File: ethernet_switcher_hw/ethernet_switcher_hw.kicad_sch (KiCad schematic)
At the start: 0 parts

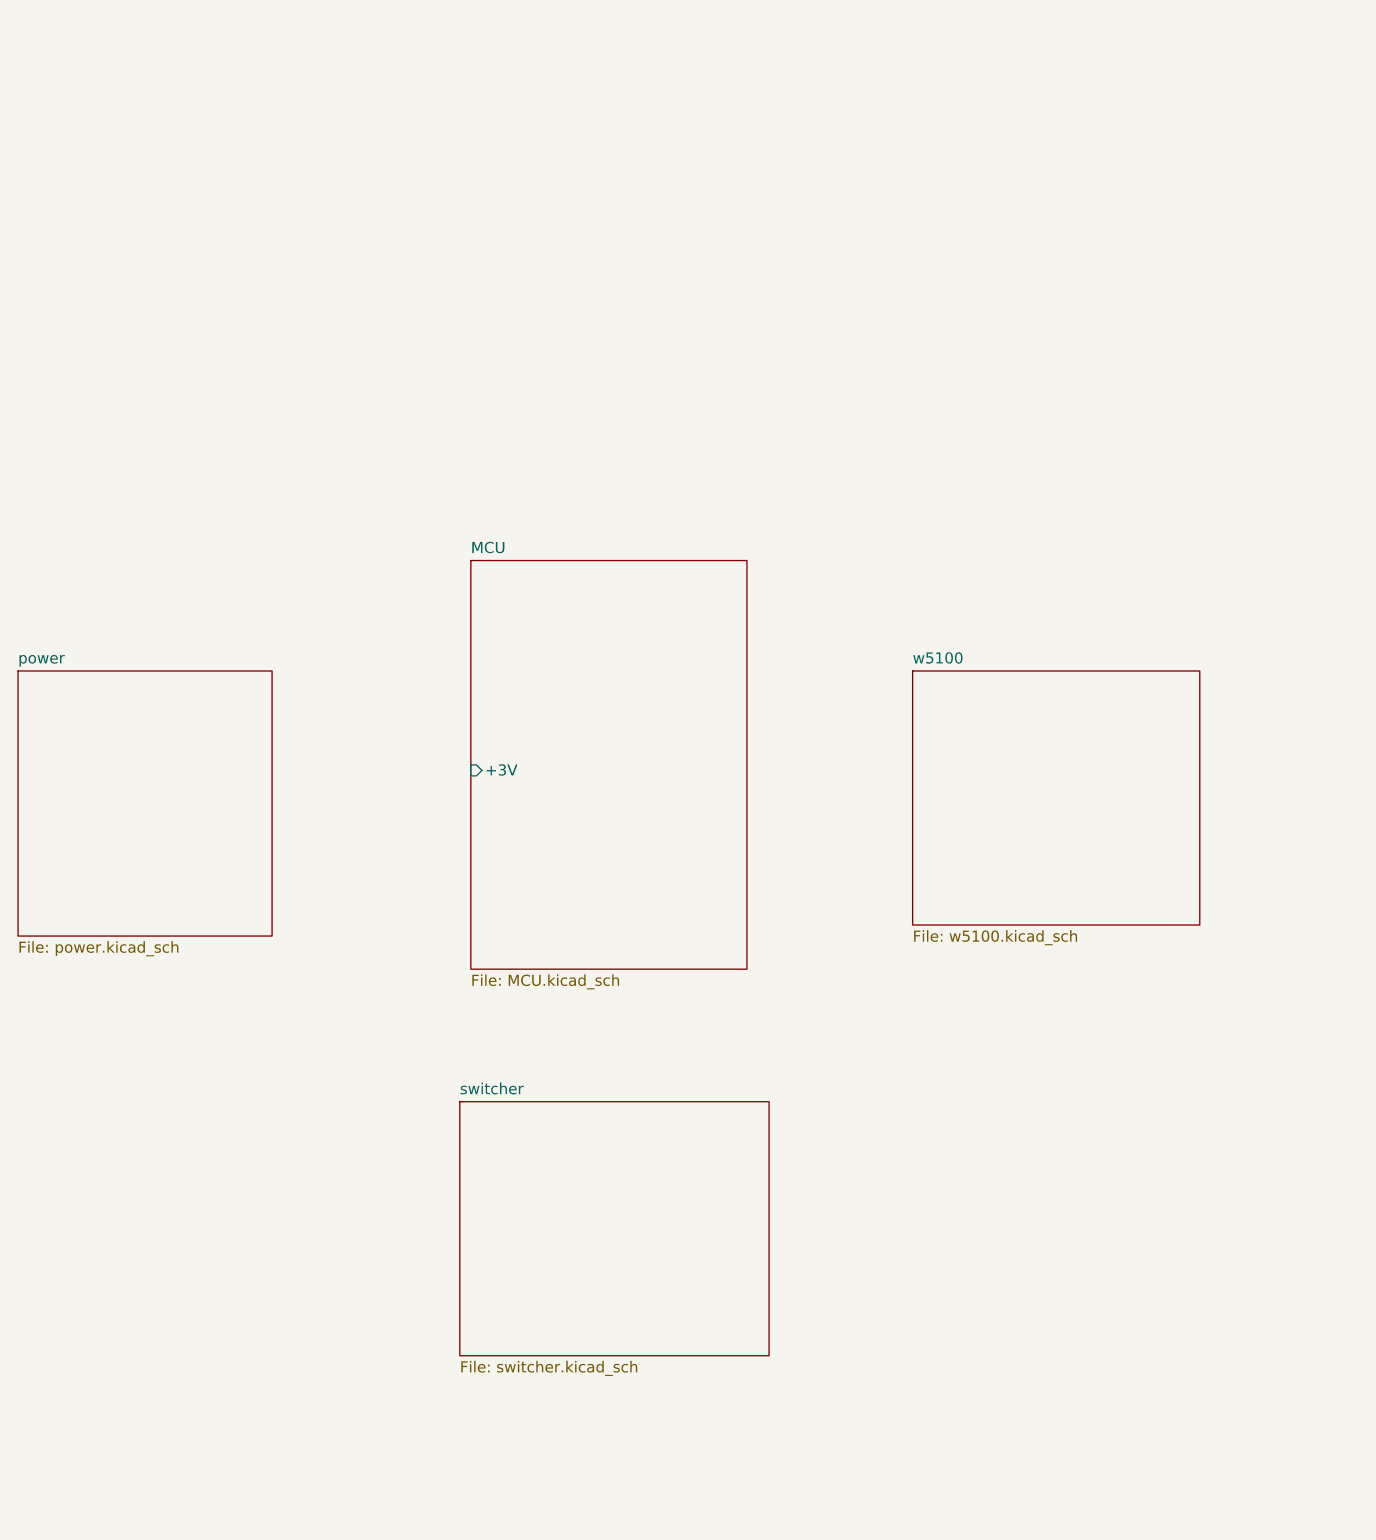
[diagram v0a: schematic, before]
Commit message: timer works incorrectly. It's clocked from slower source
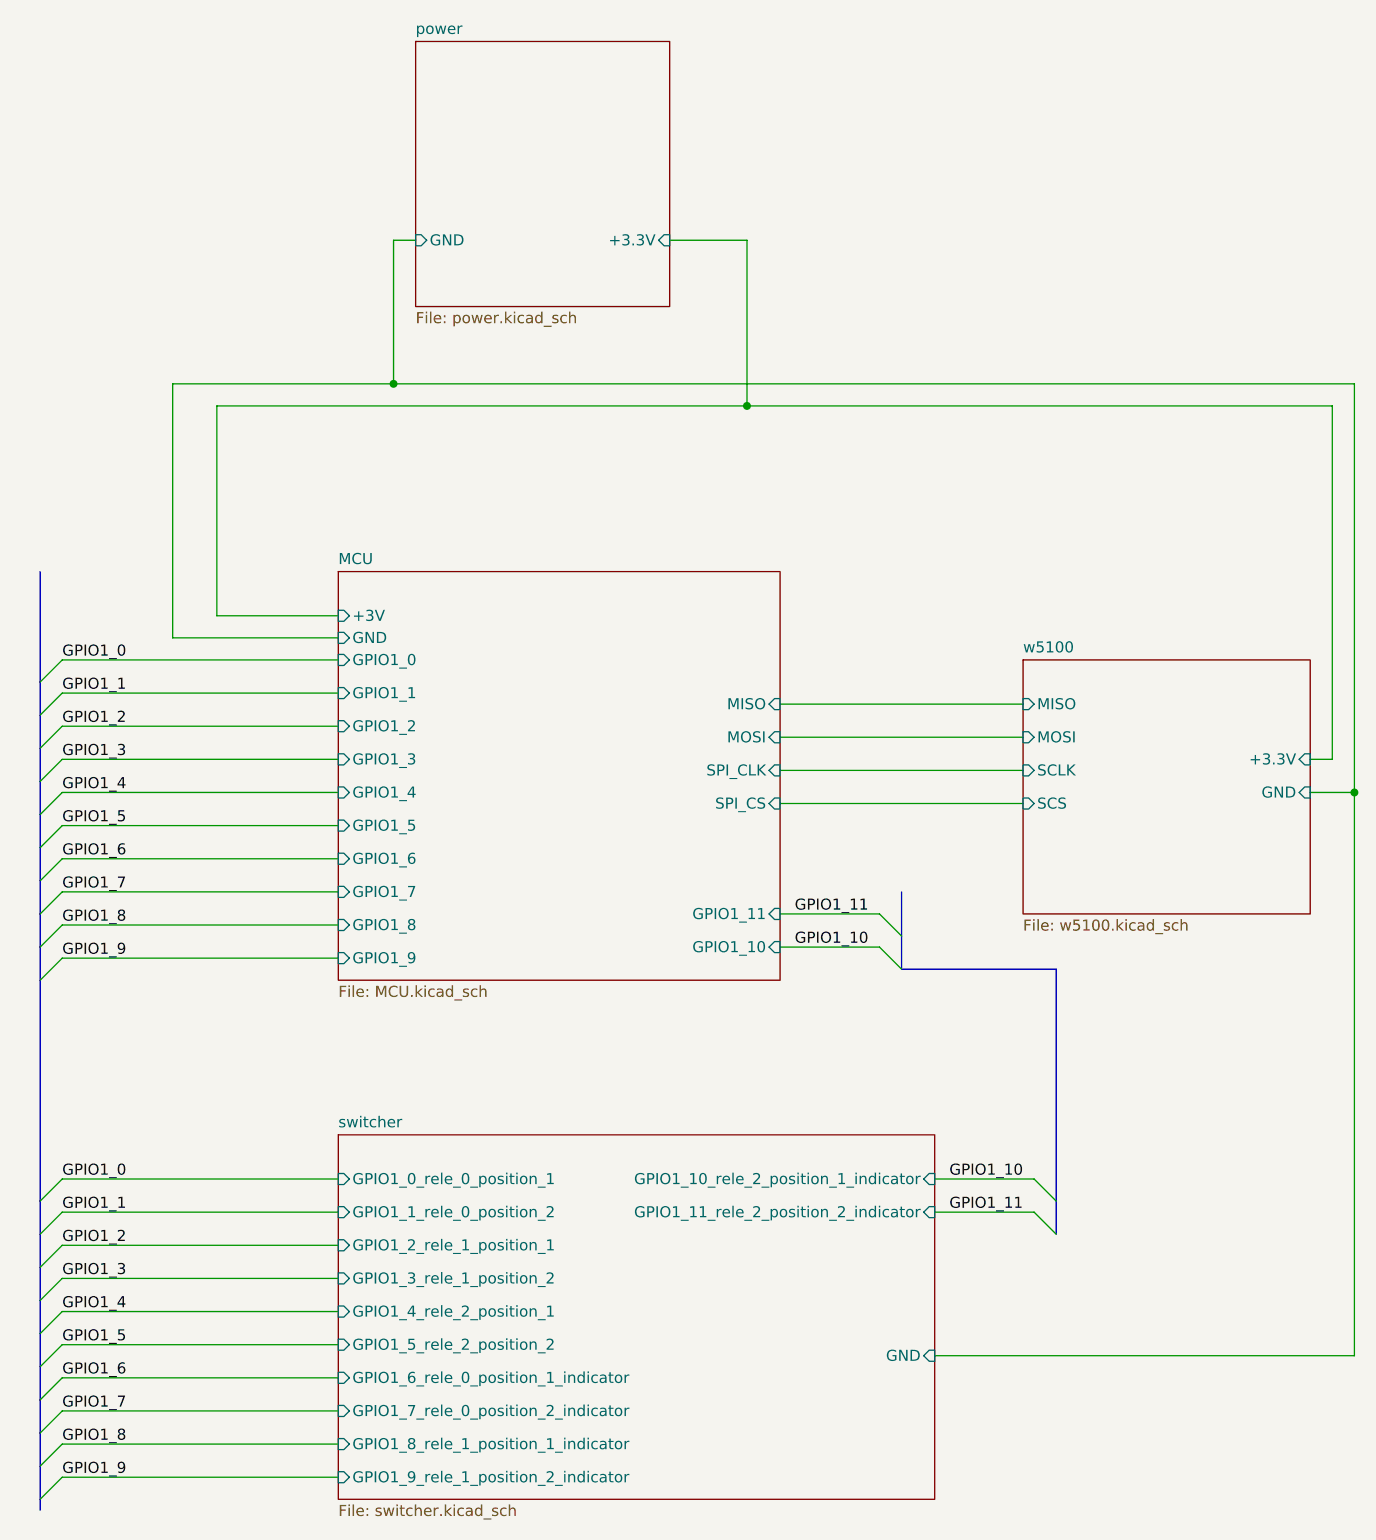
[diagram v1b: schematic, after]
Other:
- sheet MCU ports: added GND, GPIO1_0, GPIO1_1, GPIO1_10, GPIO1_11, GPIO1_2, GPIO1_3, GPIO1_4, GPIO1_5, GPIO1_6, GPIO1_7, GPIO1_8, GPIO1_9, MISO, MOSI, SPI_CLK, SPI_CS; removed none
- sheet power ports: added +3.3V, GND; removed none
- sheet switcher ports: added GND, GPIO1_0_rele_0_position_1, GPIO1_10_rele_2_position_1_indicator, GPIO1_11_rele_2_position_2_indicator, GPIO1_1_rele_0_position_2, GPIO1_2_rele_1_position_1, GPIO1_3_rele_1_position_2, GPIO1_4_rele_2_position_1, GPIO1_5_rele_2_position_2, GPIO1_6_rele_0_position_1_indicator, GPIO1_7_rele_0_position_2_indicator, GPIO1_8_rele_1_position_1_indicator, GPIO1_9_rele_1_position_2_indicator; removed none
- sheet w5100 ports: added +3.3V, GND, MISO, MOSI, SCLK, SCS; removed none

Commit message: 1.0.0. version of scheme
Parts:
- added A1: w5100_shield, forShields_footprints:forW5100Shield, symbol MIK32 Amur:w5100_shield
- added A2: MIK32 Amur, forShields_footprints:dip_MIK32_Amur, symbol MIK32 Amur:MIK32_Amur_DIP_Debug_PCB
- added C1: 680u, Capacitor_THT:CP_Radial_D16.0mm_P7.50mm, symbol Device:C_Polarized
- added C2: 330u, Capacitor_Tantalum_SMD:CP_EIA-7343-31_Kemet-D, symbol Device:C_Polarized
- added C3, C5: 0.1u, Capacitor_SMD:C_1206_3216Metric, symbol Device:C
- added C4, C6: 10u, Capacitors:CAP_1206, symbol Device:C_Polarized
- added D1: SMBJ30A, Diode_SMD:D_SMB, symbol Device:D
- added D10, D11, D12, D13, D14, D15, D16, D17, D18, D19, D20, D21, D22, D3, D4, D5, D6, D7, D8, D9: 1N4148WS, Diode_SMD:D_SOD-323F, symbol Device:D_Small
- added D2: 1N5824, Diode_THT:D_DO-201AD_P15.24mm_Horizontal, symbol Diode:1N5820
- added DD1, DD2, DD5: SN74LVCZ244APWR, Package_SO:SSOP-20_4.4x6.5mm_P0.65mm, symbol SN74LVCZ244APWR:SN74LVCZ244APWR
- added DD3: LM2596S-5.0, LM2596:LM2596SXADJ, symbol LM2596S-ADJ:LM2596S-ADJ
- added DD4: AMS1117-3.3, Package_TO_SOT_SMD:SOT-223-3_TabPin2, symbol Regulator_Linear:AMS1117-3.3
- added DD6, DD7, DD8: 74HC165, Package_SO:SOIC-16_3.9x9.9mm_P1.27mm, symbol 74xx:74HC165
- added F1: Fuse, Fuse:Fuse_0603_1608Metric, symbol Device:Fuse
- added L1: 47u, Inductor_SMD:L_12x12mm_H8mm, symbol Device:L
- added Q1, Q10, Q11, Q12, Q13, Q14, Q15, Q16, Q17, Q18, Q19, Q2, Q20, Q3, Q4, Q5, Q6, Q7, Q8, Q9: BSS138, Package_TO_SOT_SMD:SOT-23, symbol Transistor_FET:BSS138
- added R1, R12, R13, R15, R17, R20, R21, R23, R25, R28, R29, R3, R31, R33, R35, R37, R38, R5, R8, R9: 10k, Resistor_SMD:R_0603_1608Metric, symbol Device:R
- added R10, R11, R14, R16, R18, R19, R2, R22, R24, R26, R27, R30, R32, R34, R36, R39, R4, R40, R6, R7: 100k, Resistor_SMD:R_0603_1608Metric, symbol Device:R
- added R41: 20k, Resistor_SMD:R_0603_1608Metric, symbol Device:R
- added X1: Screw_Terminal_01x02, TerminalBlock_Phoenix:TerminalBlock_Phoenix_MKDS-1,5-2-5.08_1x02_P5.08mm_Horizontal, symbol Connector:Screw_Terminal_01x02
- added X2: ~, Connector_PinHeader_2.54mm:PinHeader_2x15_P2.54mm_Vertical, symbol MIK32 Amur:Connector_15_2_GOST_telemetry
- added X3: ~, Connector_PinHeader_2.54mm:PinHeader_2x15_P2.54mm_Vertical, symbol MIK32 Amur:Connector_15_2_GOST
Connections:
- net GPIO1_0: now also A2.19 (P1.0), DD1.11 (2A1), DD1.2 (1A1), DD2.11 (2A1), DD2.2 (1A1), DD5.11 (2A1), DD5.2 (1A1)
- net GPIO1_1: now also A2.18 (P1.1), DD1.13 (2A2), DD1.4 (1A2), DD2.13 (2A2), DD2.4 (1A2), DD5.13 (2A2), DD5.4 (1A2)
- net GPIO1_2: now also A2.17 (P1.2), DD1.15 (2A3), DD1.6 (1A3), DD2.15 (2A3), DD2.6 (1A3), DD5.15 (2A3), DD5.6 (1A3)
- net GPIO1_3: now also A2.16 (P1.3), DD1.17 (2A4), DD1.8 (1A4), DD2.17 (2A4), DD2.8 (1A4), DD5.17 (2A4), DD5.8 (1A4)
- net GPIO1_4: now also A2.15 (P1.4), DD8.9 (Q)
- net GPIO1_5: now also A2.14 (P1.5), DD6.1 (~{PL}), DD7.1 (~{PL}), DD8.1 (~{PL})
- net GPIO1_6: now also A2.13 (P1.6), DD6.15 (~{CE}), DD7.15 (~{CE}), DD8.15 (~{CE})
- net GPIO1_7: now also A2.12 (P1.7), DD2.19 (2~{OE})
- net GPIO1_8: now also A2.11 (P1.8), DD5.1 (1~{OE})
- net GPIO1_9: now also A2.10 (P1.9), DD5.19 (2~{OE})
- new net: Q2.1 (G), R3.1, R4.1
- new net: Q15.1 (G), R29.1, R30.1
- new net: Q16.1 (G), R31.1, R32.1
- new net: D3.1 (K), D5.1 (K), X3.3 (r1p0)
- new net: Q18.1 (G), R35.1, R36.1
- new net: Q13.1 (G), R25.1, R26.1
- new net: Q9.1 (G), R17.1, R18.1
- new net: Q12.1 (G), R23.1, R24.1
- new net: Q17.1 (G), R33.1, R34.1
- new net: Q1.1 (G), R1.1, R2.1
- new net: Q3.1 (G), R5.1, R6.1
- new net: Q4.1 (G), R7.1, R8.1
- new net: D16.1 (K), D18.1 (K), X3.27 (r9p1)
- new net: Q11.1 (G), R21.1, R22.1
- new net: D7.1 (K), D9.1 (K), X3.6 (r2p1)
- new net: D10.1 (K), D8.1 (K), X3.21 (+3.3V)
- new net: Q14.1 (G), R27.1, R28.1
- new net: Q20.1 (G), R38.1, R40.1
- new net: Q7.1 (G), R13.1, R14.1
- new net: Q19.1 (G), R37.1, R39.1
- new net: D12.1 (K), D14.1 (K), X3.24 (+3.3V)
- new net: C1.1, D1.1 (K), DD3.1 (VIN), F1.2
- new net: D19.1 (K), D21.1 (K), X3.15 (+3.3V)
- new net: Q8.1 (G), R15.1, R16.1
- new net: D15.1 (K), D17.1 (K), X3.12 (r5p1)
- new net: D2.1 (K), DD3.2 (OUTPUT), L1.1
- new net: Q10.1 (G), R19.1, R20.1
- new net: D4.1 (K), D6.1 (K), X3.18 (+3.3V)
- new net: D11.1 (K), D13.1 (K), X3.9 (r4p0)
- new net: Q6.1 (G), R11.1, R12.1
- new net: A1.5 (+5V), A2.43 (P0.4)
- new net: A1.8 (CLK), A2.45 (P0.2)
- new net: A1.3 (MOSI), A2.46 (P0.1)
- new net: A1.7 (MISO), A2.47 (P0.0)
- new net: D20.1 (K), D22.1 (K), X3.30 (+3.3V)
- new net: Q5.1 (G), R10.1, R9.1
- new net: F1.1, X1.2 (Pin_2)
- new net +3.3V: A2.1 (3V3), C5.1, C6.1, DD1.20 (VCC), DD2.20 (VCC), DD4.2 (VO), DD5.20 (VCC), X2.12 (r5t1), X2.15 (+3.3V), X2.18 (+3.3V), X2.21 (+3.3V), X2.24 (+3.3V), X2.27 (r9t1), X2.3 (r1t0), X2.30 (+3.3V), X2.6 (r2t1), X2.9 (r4t0)
- new net +5V: A1.4 (NSS), C2.1, C3.1, C4.1, DD3.4 (FEED_BACK), DD4.3 (VI), DD6.16 (VCC), DD7.16 (VCC), DD8.16 (VCC), L1.2
- new net GND: A1.10 (GND), A1.2 (GND), A2.25 (GND), C1.2, C2.2, C3.2, C4.2, C5.2, C6.2, D1.2 (A), D2.2 (A), DD1.10 (GND), DD2.10 (GND), DD3.3 (GND_1), DD3.5 (~{ON}/OFF), DD3.T1 (GND_2), DD3.T2 (GND_3), DD4.1 (GND), DD5.10 (GND), DD6.8 (GND), DD7.8 (GND), DD8.8 (GND), Q1.2 (S), Q10.2 (S), Q11.2 (S), Q12.2 (S), Q13.2 (S), Q14.2 (S), Q15.2 (S), Q16.2 (S), Q17.2 (S), Q18.2 (S), Q19.2 (S), Q2.2 (S), Q20.2 (S), Q3.2 (S), Q4.2 (S), Q5.2 (S), Q6.2 (S), Q7.2 (S), Q8.2 (S), Q9.2 (S), R10.2, R11.2, R14.2, R16.2, R18.2, R19.2, R2.2, R22.2, R24.2, R26.2, R27.2, R30.2, R32.2, R34.2, R36.2, R39.2, R4.2, R40.2, R6.2, R7.2, X1.1 (Pin_1)
- new net GPIO0_10: A2.35 (P0.10), DD2.1 (1~{OE}), R41.2
- new net GPIO0_7: A2.38 (P0.7), DD6.2 (CLK), DD7.2 (CLK), DD8.2 (CLK)
- new net GPIO0_8: A2.37 (P0.8), DD1.1 (1~{OE})
- new net GPIO0_9: A2.36 (P0.9), DD1.19 (2~{OE})
- new net r0p0: D3.2 (A), X3.1 (rop0)
- new net r0p1: D5.2 (A), Q2.3 (D), X3.2 (rop1)
- new net r0p1_ctrl: DD1.18 (1Y1), R3.2
- new net r0p2: Q4.3 (D)
- new net r0p2_ctrl: DD1.16 (1Y2), R8.2
- new net r0t0: DD8.11 (D0), X2.1 (rot0)
- new net r0t1: DD8.12 (D1), X2.2 (rot1)
- new net r1p0: D7.2 (A), X3.3 (r1p0)
- new net r1p1: D9.2 (A), Q6.3 (D), X3.4 (r1p1)
- new net r1p1_ctrl: DD1.14 (1Y3), R12.2
- new net r1p2: Q8.3 (D)
- new net r1p2_ctrl: DD1.12 (1Y4), R15.2
- new net r1t0: DD8.13 (D2), X2.3 (r1t0)
- new net r1t1: DD8.14 (D3), X2.4 (r1t1)
- new net r2p0: D11.2 (A), X3.5 (r2p0)
- new net r2p1: D13.2 (A), Q10.3 (D), X3.6 (r2p1)
- new net r2p1_ctrl: DD1.9 (2Y1), R20.2
- new net r2p2: Q12.3 (D)
- new net r2p2_ctrl: DD1.7 (2Y2), R23.2
- new net r2t0: DD8.3 (D4), X2.5 (r2t0)
- new net r2t1: DD8.4 (D5), X2.6 (r2t1)
- new net r3p0: D15.2 (A), X3.7 (r3p0)
- new net r3p1: D17.2 (A), Q14.3 (D), X3.8 (r3p1)
- new net r3p1_ctrl: DD1.5 (2Y3), R28.2
- new net r3p2: Q16.3 (D)
- new net r3p2_ctrl: DD1.3 (2Y4), R31.2
- new net r3t0: DD8.5 (D6), X2.7 (r3t0)
- new net r3t1: DD8.6 (D7), X2.8 (r3t1)
- new net r4p0: D19.2 (A), X3.9 (r4p0)
- new net r4p1: D21.2 (A), Q18.3 (D), X3.10 (r4p1)
- new net r4p1_ctrl: DD2.18 (1Y1), R35.2
- new net r4p2: Q19.3 (D)
- new net r4p2_ctrl: DD2.16 (1Y2), R37.2
- new net r4t0: DD7.11 (D0), X2.9 (r4t0)
- new net r4t1: DD7.12 (D1), X2.10 (r4t1)
- new net r5p0: D4.2 (A), X3.11 (r5p0)
- new net r5p1: D6.2 (A), Q1.3 (D), X3.12 (r5p1)
- new net r5p1_ctrl: DD2.14 (1Y3), R1.2
- new net r5p2: Q3.3 (D)
- new net r5p2_ctrl: DD2.12 (1Y4), R5.2
- new net r5t0: DD7.13 (D2), X2.11 (r5t0)
- new net r5t1: DD7.14 (D3), X2.12 (r5t1)
- new net r6p0: D8.2 (A), X3.13 (r6p0)
- new net r6p1: D10.2 (A), Q5.3 (D), X3.14 (r6p1)
- new net r6p1_ctrl: DD2.9 (2Y1), R9.2
- new net r6p2: Q7.3 (D)
- new net r6p2_ctrl: DD2.7 (2Y2), R13.2
- new net r6t0: DD7.3 (D4), X2.13 (r6t0)
- new net r6t1: DD7.4 (D5), X2.14 (r6t1)
- new net r7p0: D12.2 (A), X3.22 (r7p0)
- new net r7p1: D14.2 (A), Q9.3 (D), X3.23 (r7p1)
- new net r7p1_ctrl: DD2.5 (2Y3), R17.2
- new net r7p2: Q11.3 (D)
- new net r7p2_ctrl: DD2.3 (2Y4), R21.2
- new net r7t0: DD7.5 (D6), X2.22 (r7t0)
- new net r7t1: DD7.6 (D7), DD8.10 (DS), X2.23 (r7t1)
- new net r8p0: D16.2 (A), X3.25 (r8p0)
- new net r8p1: D18.2 (A), Q13.3 (D), X3.26 (r9p0)
- new net r8p1_ctrl: DD5.18 (1Y1), R25.2
- new net r8p2: Q15.3 (D)
- new net r8p2_ctrl: DD5.16 (1Y2), R29.2
- new net r8t0: DD6.3 (D4), X2.25 (r8t0)
- new net r8t1: DD6.4 (D5), X2.26 (r9t0)
- new net r9p0: D20.2 (A), X3.26 (r9p0)
- new net r9p1: D22.2 (A), Q17.3 (D), X3.27 (r9p1)
- new net r9p1_ctrl: DD5.14 (1Y3), R33.2
- new net r9p2: Q20.3 (D)
- new net r9p2_ctrl: DD5.12 (1Y4), R38.2
- new net r9t0: DD6.5 (D6), X2.26 (r9t0)
- new net r9t1: DD6.6 (D7), DD7.10 (DS), X2.27 (r9t1)
- no-connect marks 0 -> 45
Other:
- removed sheet MCU
- removed sheet power
- removed sheet switcher
- removed sheet w5100
- note added: "CONTROL_SIGNALS"
- note added: "MCU"
- note added: "POWER"
- note added: "TELEMETRY"

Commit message: ready project
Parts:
- added Q17, Q20, Q21, Q24: NPN, Package_TO_SOT_SMD:SOT-23_Handsoldering, symbol Simulation_SPICE:NPN
- added R10, R16, R25, R26, R41, R49, R62, R69, R9: 20k, Resistor_SMD:R_0603_1608Metric, symbol Device:R
- added R39, R42, R53, R67: 4.7k, Resistor_SMD:R_0603_1608Metric, symbol Device:R
- added R40, R47, R58, R68: 1k, Resistor_SMD:R_0603_1608Metric, symbol Device:R
- added R48, R50, R51, R52, R54, R55, R56, R57, R59, R60, R61, R70, R71, R72, R73, R74, R75, R76, R77, R78: 100k, Resistor_SMD:R_0603_1608Metric, symbol Device:R
- DD1, DD2, DD5: footprint Package_SO:SSOP-20_4.4x6.5mm_P0.65mm -> Package_DIP:DIP-20_W7.62mm
- DD6, DD7, DD8: footprint Package_SO:SOIC-16_3.9x9.9mm_P1.27mm -> Package_DIP:DIP-16_W7.62mm
- Q1, Q10, Q11, Q12, Q13, Q14, Q15, Q16, Q2, Q3, Q4, Q5, Q6, Q7, Q8, Q9: value BSS138 -> AO3422A; footprint Package_TO_SOT_SMD:SOT-23 -> Package_TO_SOT_SMD:SOT-23_Handsoldering
- Q18: renamed from Q17; value BSS138 -> AO3422A; footprint Package_TO_SOT_SMD:SOT-23 -> Package_TO_SOT_SMD:SOT-23_Handsoldering
- Q19: renamed from Q18; value BSS138 -> AO3422A; footprint Package_TO_SOT_SMD:SOT-23 -> Package_TO_SOT_SMD:SOT-23_Handsoldering
- Q22: renamed from Q19; value BSS138 -> AO3422A; footprint Package_TO_SOT_SMD:SOT-23 -> Package_TO_SOT_SMD:SOT-23_Handsoldering
- Q23: renamed from Q20; value BSS138 -> AO3422A; footprint Package_TO_SOT_SMD:SOT-23 -> Package_TO_SOT_SMD:SOT-23_Handsoldering
- R1, R3, R5, R8: value 10k -> 100
- R11: renamed from R9; value 10k -> 100
- R14: renamed from R12; value 10k -> 100
- R17: renamed from R13; value 10k -> 100
- R19: renamed from R15; value 10k -> 100
- R21: renamed from R17; value 10k -> 100
- R24: renamed from R20; value 10k -> 100
- R27: renamed from R21; value 10k -> 100
- R29: renamed from R23; value 10k -> 100
- R31: renamed from R25; value 10k -> 100
- R34: renamed from R28; value 10k -> 100
- R35: renamed from R29; value 10k -> 100
- R37: renamed from R31; value 10k -> 100
- R43: renamed from R33; value 10k -> 100
- R45: renamed from R35; value 10k -> 100
- R63: renamed from R37; value 10k -> 100
- R64: renamed from R38; value 10k -> 100
- renumbered R10 to R12, R11 to R13, R41 to R15, R14 to R18, R16 to R20, R18 to R22, R19 to R23, R22 to R28, R24 to R30, R26 to R32, R27 to R33, R30 to R36, R32 to R38, R34 to R44, R36 to R46, R39 to R65, R40 to R66
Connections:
- net r0p0 is gone; now on net r0p1: D3.2 (A), X3.1 (rop0)
- net r7p0 is gone; now on net r7p1: D12.2 (A), X3.22 (r7p0)
- net r8p0 is gone; now on net r8p1: D16.2 (A), X3.25 (r8p0)
- net +3.3V: now also D10.1 (K), D11.1 (K), D12.1 (K), D13.1 (K), D14.1 (K), D15.1 (K), D16.1 (K), D17.1 (K), D18.1 (K), D19.1 (K), D20.1 (K), D21.1 (K), D22.1 (K), D3.1 (K), D4.1 (K), D5.1 (K), D6.1 (K), D7.1 (K), D8.1 (K), D9.1 (K), X3.12 (+3.3V), X3.15 (+3.3V), X3.18 (+3.3V), X3.21 (+3.3V), X3.24 (+3.3V), X3.27 (+3.3V), X3.3 (+3.3V), X3.30 (+3.3V), X3.6 (+3.3V), X3.9 (+3.3V), R41.2, R49.2, R62.2, R69.2; no longer DD1.20 (VCC), DD2.20 (VCC), DD5.20 (VCC)
- net +5V: now also DD1.20 (VCC), DD2.20 (VCC), DD5.20 (VCC), R15.1, R10.1, R16.1, R25.1, R26.1, R39.1, R42.1, R53.1, R67.1, R9.1
- net GND: now also Q17.3 (E), Q20.3 (E), Q21.3 (E), Q24.3 (E), R48.1, R50.1, R51.1, R52.1, R54.1, R55.1, R56.1, R57.1, R59.1, R60.1, R61.1, R70.1, R71.1, R72.1, R73.1, R74.1, R75.1, R76.1, R77.1, R78.1
- net GPIO0_8: now also R9.2
- net GPIO0_9: now also R10.2
- net GPIO1_0: now also R40.2, R41.1; no longer DD1.11 (2A1), DD1.2 (1A1), DD2.11 (2A1), DD2.2 (1A1), DD5.11 (2A1), DD5.2 (1A1)
- net GPIO1_1: now also R47.2, R49.1; no longer DD1.13 (2A2), DD1.4 (1A2), DD2.13 (2A2), DD2.4 (1A2), DD5.13 (2A2), DD5.4 (1A2)
- net GPIO1_2: now also R58.2, R62.1; no longer DD1.15 (2A3), DD1.6 (1A3), DD2.15 (2A3), DD2.6 (1A3), DD5.15 (2A3), DD5.6 (1A3)
- net GPIO1_3: now also R68.2, R69.1; no longer DD1.17 (2A4), DD1.8 (1A4), DD2.17 (2A4), DD2.8 (1A4), DD5.17 (2A4), DD5.8 (1A4)
- net GPIO1_7: now also R16.2
- net GPIO1_8: now also R25.2
- net GPIO1_9: now also R26.2
- net r0p1: no longer D5.2 (A), X3.2 (rop1)
- net r0p2: now also D5.2 (A), X3.2 (rop1)
- net r0t0: now also R57.2
- net r0t1: now also R54.2
- net r1p1: now also D7.2 (A); no longer D9.2 (A)
- net r1p2: now also D9.2 (A), X3.5 (r1p1)
- net r1t0: now also X2.4 (r1t0), R51.2; no longer X2.3 (r1t0)
- net r1t1: now also X2.5 (r1t1), R48.2; no longer X2.4 (r1t1)
- net r2p1: now also D11.2 (A), X3.7 (r2p0); no longer D13.2 (A), X3.6 (r2p1)
- net r2p2: now also D13.2 (A), X3.8 (r2p1)
- net r2t0: now also X2.7 (r2t0), R71.2; no longer X2.5 (r2t0)
- net r2t1: now also X2.8 (r2t1), R73.2; no longer X2.6 (r2t1)
- net r3p1: now also D15.2 (A), X3.10 (r3p0); no longer D17.2 (A), X3.8 (r3p1)
- net r3p2: now also D17.2 (A), X3.11 (r3p1)
- net r3t0: now also X2.10 (r3t0), R75.2; no longer X2.7 (r3t0)
- net r3t1: now also X2.11 (r3t1), R77.2; no longer X2.8 (r3t1)
- net r4p1: now also D19.2 (A), X3.13 (r4p0); no longer D21.2 (A), X3.10 (r4p1)
- net r4p2: now also D21.2 (A), X3.14 (r4p1)
- net r4t0: now also X2.13 (r4t0), R61.2; no longer X2.9 (r4t0)
- net r4t1: now also X2.14 (r4t1), R60.2; no longer X2.10 (r4t1)
- net r5p1: now also D4.2 (A), X3.16 (r5p0); no longer D6.2 (A), X3.12 (r5p1)
- net r5p2: now also D6.2 (A), X3.17 (r5p1)
- net r5t0: now also X2.16 (r5t0), R59.2; no longer X2.11 (r5t0)
- net r5t1: now also X2.17 (r5t1), R56.2; no longer X2.12 (r5t1)
- net r6p1: now also D8.2 (A), X3.19 (r6p0); no longer D10.2 (A), X3.14 (r6p1)
- net r6p2: now also D10.2 (A), X3.20 (r6p1)
- net r6t0: now also X2.19 (r6t0), R55.2; no longer X2.13 (r6t0)
- net r6t1: now also X2.20 (r6t1), R52.2; no longer X2.14 (r6t1)
- net r7p1: no longer D14.2 (A), X3.23 (r7p1)
- net r7p2: now also D14.2 (A), X3.23 (r7p1)
- net r7t0: now also R50.2
- net r7t1: now also R70.2
- net r8p1: no longer D18.2 (A), X3.26 (r9p0)
- net r8p2: now also D18.2 (A), X3.26 (r8p1)
- net r8t0: now also R72.2
- net r8t1: now also R74.2
- net r9p1: now also D20.2 (A), X3.28 (r9p0); no longer D22.2 (A), X3.27 (r9p1)
- net r9p2: now also D22.2 (A), X3.29 (r9p1)
- net r9t0: now also X2.28 (r9t0), R76.2; no longer X2.26 (r9t0)
- net r9t1: now also X2.29 (r9t1), R78.2; no longer X2.27 (r9t1)
- removed net r1p0: D7.2 (A), X3.3 (r1p0)
- removed net r2p0: D11.2 (A), X3.5 (r2p0)
- removed net r3p0: D15.2 (A), X3.7 (r3p0)
- removed net r4p0: D19.2 (A), X3.9 (r4p0)
- removed net r5p0: D4.2 (A), X3.11 (r5p0)
- removed net r6p0: D8.2 (A), X3.13 (r6p0)
- removed net r9p0: D20.2 (A), X3.26 (r9p0)
- new net: Q20.2 (B), R47.1
- new net: Q21.2 (B), R58.1
- new net: Q17.2 (B), R40.1
- new net: Q24.2 (B), R68.1
- new net line0_ctrl: DD1.11 (2A1), DD1.2 (1A1), DD2.11 (2A1), DD2.2 (1A1), DD5.11 (2A1), DD5.2 (1A1), Q17.1 (C), R39.2
- new net line1_ctrl: DD1.13 (2A2), DD1.4 (1A2), DD2.13 (2A2), DD2.4 (1A2), DD5.13 (2A2), DD5.4 (1A2), Q20.1 (C), R42.2
- new net line2_ctrl: DD1.15 (2A3), DD1.6 (1A3), DD2.15 (2A3), DD2.6 (1A3), DD5.15 (2A3), DD5.6 (1A3), Q21.1 (C), R53.2
- new net line3_ctrl: DD1.17 (2A4), DD1.8 (1A4), DD2.17 (2A4), DD2.8 (1A4), DD5.17 (2A4), DD5.8 (1A4), Q24.1 (C), R67.2
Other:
- moved on the sheet: DD6, DD7, DD8
